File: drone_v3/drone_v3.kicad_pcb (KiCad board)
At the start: 2 copper layers, 47.5 x 47.5 mm, 85 parts, among them J1 USB_B_Micro, J10 Conn_01x08_Male, J12 Conn_01x08_Male, J13 Conn_01x08_Male, J14 Conn_01x02_Male, J15 UART4_con, J16 Conn_01x03_Male, J17 Conn_01x02_Male, J18 Conn_01x03_Male, J19 Micro_SD_Card, J2 Conn_01x10_Female, J3 UART4_con, J4 Conn_01x04_Male, J5 Conn_01x02_Female, J6 Conn_01x04_Male, J7 Conn_01x04_Male, J8 UART4_con, J9 Conn_01x06_Male, Q1 2N3904, Q2 2N3904, SW1 SW_Push, U1 STM32F405RGTx, U2 USBLC6-2SC6, U3 MPU-9250, U4 MCP1700-3302E_SOT23, U5 24LC512, U6 NRF24L01_Breakout, U7 MS5611-01BA, U8 ICM-20602, U9 MCP1700-3302E_SOT23, Y1 Crystal_GND24

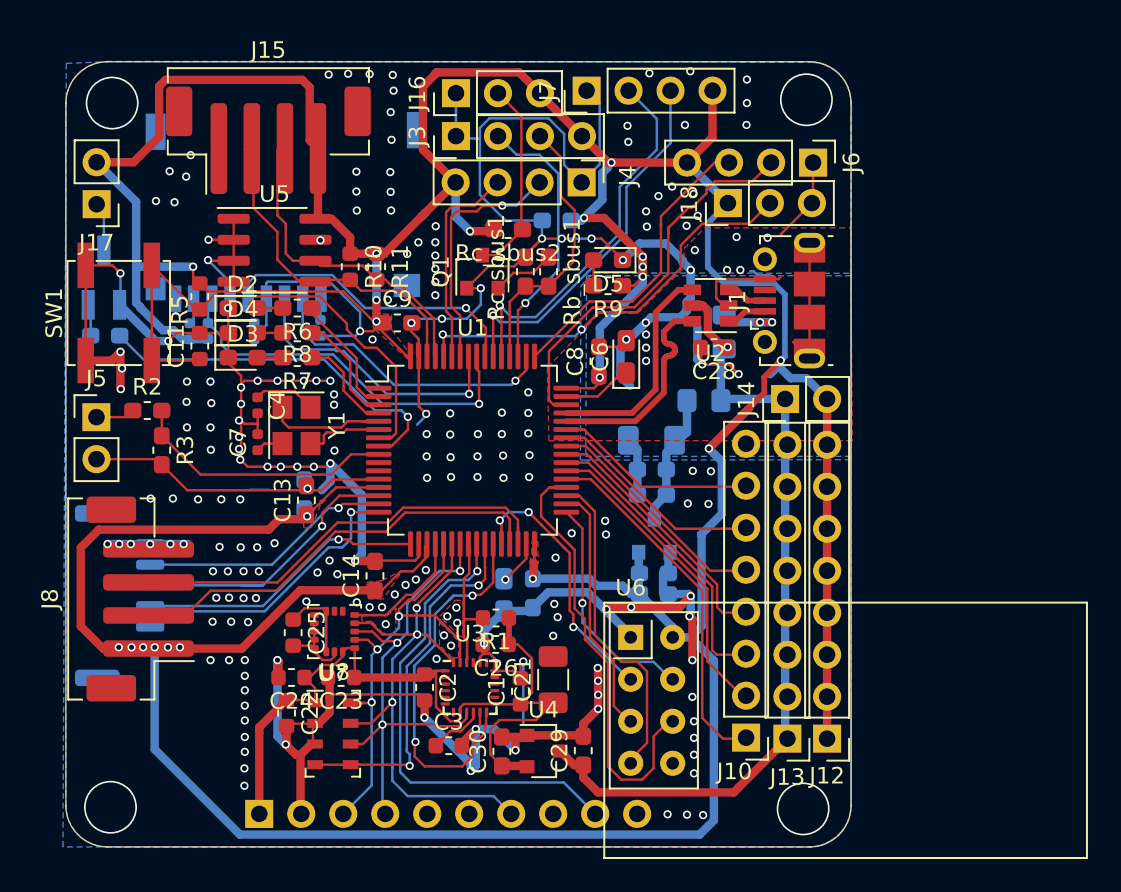
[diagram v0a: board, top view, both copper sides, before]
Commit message: cystal layout
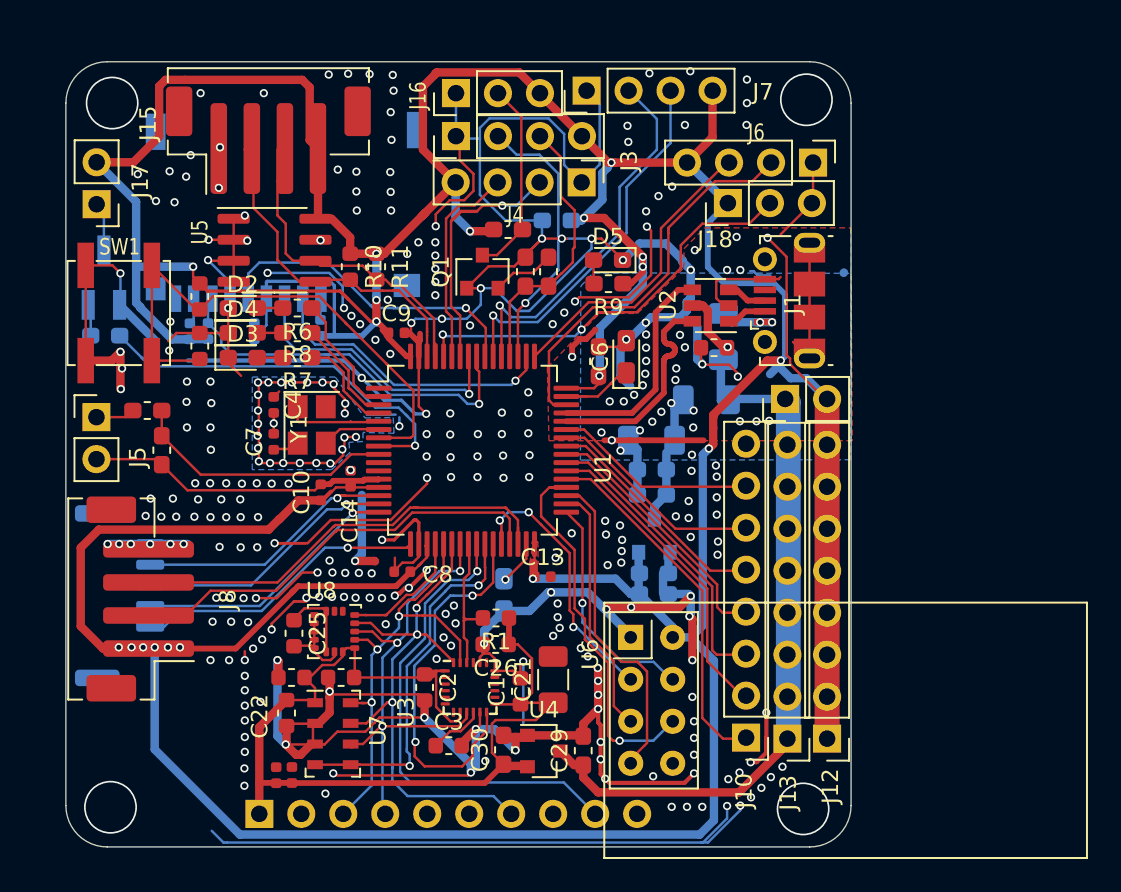
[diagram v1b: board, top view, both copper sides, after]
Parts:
- added C27: 1uF, Capacitor_SMD:C_0402_1005Metric, F.Cu at (118.7, 125.7)
- added C31: 100nF, Capacitor_SMD:C_0402_1005Metric, F.Cu at (117.7, 125.7)
- C10: footprint Capacitor_SMD:C_0603_1608Metric_Pad1.05x0.95mm_HandSolder -> Capacitor_SMD:C_0402_1005Metric; moved to F.Cu
- C13, C14, C8, C9: footprint Capacitor_SMD:C_0603_1608Metric_Pad1.05x0.95mm_HandSolder -> Capacitor_SMD:C_0402_1005Metric
- C20: moved to F.Cu
- D1, D6: footprint Diode_SMD:D_0805_2012Metric_Pad1.15x1.40mm_HandSolder -> Diode_SMD:D_1206_3216Metric
- moved C8 17.4 mm to (125.3, 113.3), turned to 180 degrees
- moved C13 15.0 mm to (133.8, 113.7), turned to 0 degrees
- moved C20 14.6 mm to (137.2, 100.6), turned to 90 degrees
- moved G*** 8.81 mm to (136.8, 104.0)
- moved C14 6.06 mm to (122.2, 107.7)
- moved C10 1.01 mm to (120.4, 108.5)
- moved C7 0.98 mm to (117.6, 105.5)
- moved C4 0.98 mm to (117.6, 103.3)
- moved Y1 0.93 mm to (119.9, 104.5)
- moved C9 0.60 mm to (125.0, 98.9)
- moved D6 0.28 mm to (144.8, 99.1)
- moved D1 0.16 mm to (143.8, 103.0)
- moved C30 0.14 mm to (131.5, 124.1)
- moved R9 0.13 mm to (137.8, 95.9)
- moved C25 0.06 mm to (118.8, 117.1)
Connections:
- J1 pad 6: Net-(J1-Pad6) -> GND
- J9 pad 2: UART2_TX -> UART2_RX
- J9 pad 3: UART2_RX -> UART2_TX
- J9 pad 4: UART2_CTS -> UART2_RTS
- J9 pad 5: UART2_RTS -> UART2_CTS
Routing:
- net GND: track 297.3 -> 479.4 mm, vias 211 -> 311
- net +3.3VA: track 49.3 -> 62.1 mm
- net Net-(J1-Pad6): track 7.21 -> 0.00 mm
- net VCC: track 315.4 -> 320.4 mm, vias 22 -> 19
- net SPI2_MOSI: track 27.4 -> 23.4 mm, vias 0 -> 1
- net Net-(C4-Pad1): track 3.94 -> 0.64 mm
- net OSC1+: track 7.96 -> 5.01 mm
- net Buzzer: track 22.4 -> 24.8 mm
- net NRST: track 32.0 -> 34.2 mm
- net SD_CLK: track 18.9 -> 20.9 mm
- net UART2_CTS: track 17.7 -> 15.7 mm
- net UART2_TX: track 17.6 -> 16.3 mm
- net (no net): track 1.33 -> 0.03 mm
- net OSC1-: track 4.81 -> 3.58 mm
- net Net-(C15-Pad1): track 7.99 -> 6.97 mm
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
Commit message: crystal layout
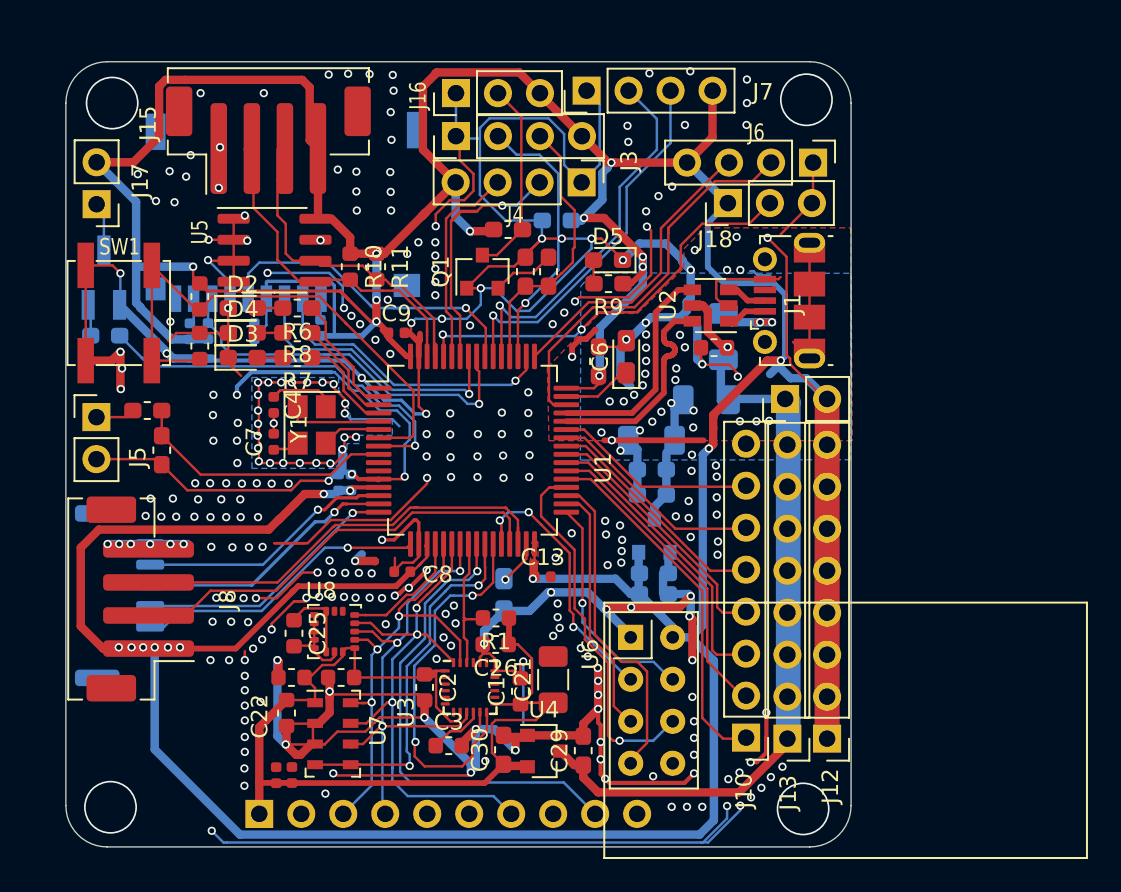
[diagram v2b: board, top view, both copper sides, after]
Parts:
- C10, C14: moved to B.Cu
- moved C10 1.23 mm to (121.5, 108.0)
- moved C14 0.23 mm to (122.2, 108.0)
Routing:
- net GND: track 479.4 -> 501.8 mm, vias 311 -> 313
- net Net-(C4-Pad1): track 0.64 -> 4.69 mm
- net VCC: track 320.4 -> 320.7 mm, vias 19 -> 21

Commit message: change 20602 to 20948, ms5611 to bmp180
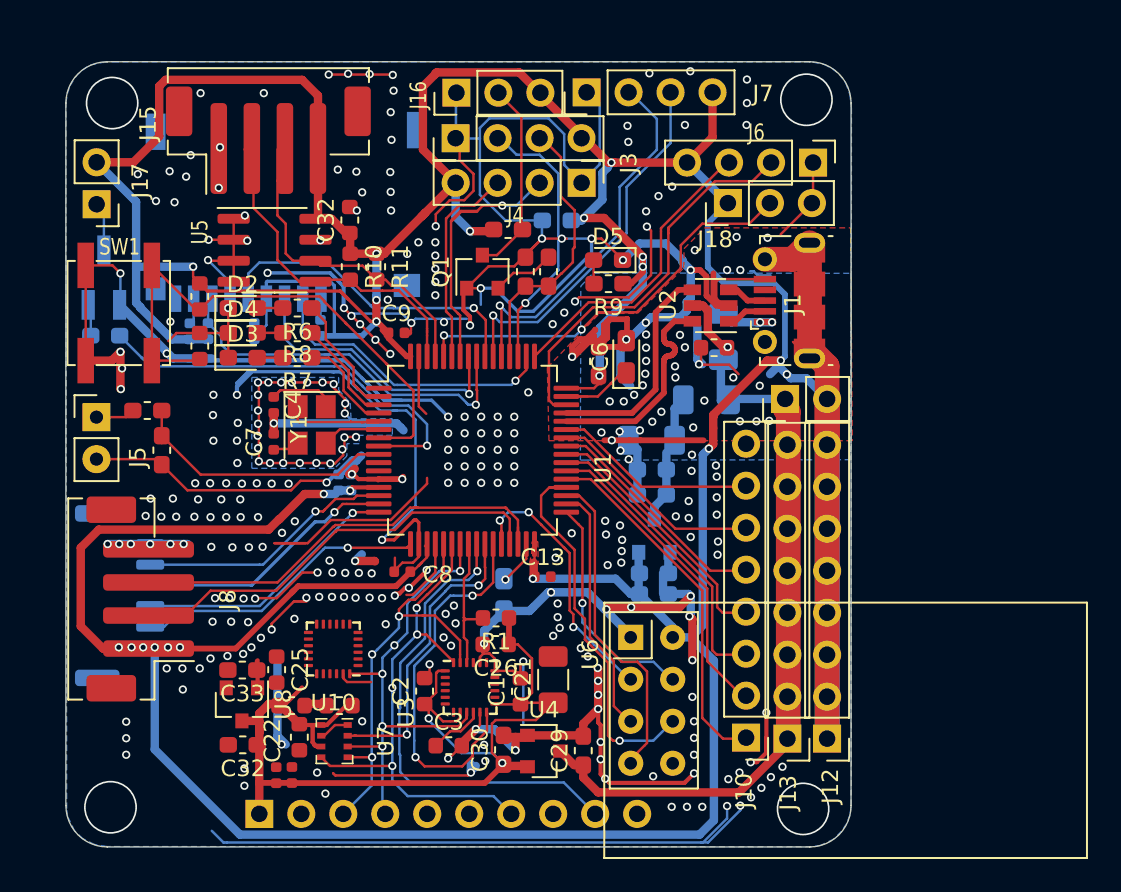
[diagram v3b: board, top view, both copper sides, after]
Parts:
- added C32: 1uF, Capacitor_SMD:C_0603_1608Metric_Pad1.05x0.95mm_HandSolder, F.Cu at (115.7, 123.8)
- added C32: C, Capacitor_SMD:C_0603_1608Metric, F.Cu at (122.2, 92.1)
- added C33: 1uF, Capacitor_SMD:C_0603_1608Metric_Pad1.05x0.95mm_HandSolder, F.Cu at (115.7, 119.3)
- added U10: ICM-20948, Sensor_Motion:InvenSense_QFN-24_3x3mm_P0.4mm, F.Cu at (121.2, 118.0)
- U7: value MS5611-01BA -> BMP280; footprint Package_LGA:LGA-8_3x5mm_P1.25mm -> Package_LGA:Bosch_LGA-8_2x2.5mm_P0.65mm_ClockwisePinNumbering
- U8: value ICM-20602 -> MCP1804x-1802xDB; footprint Package_LGA:LGA-16_3x3mm_P0.5mm_LayoutBorder3x5y -> Package_TO_SOT_SMD:SOT-23
- moved G*** 11.2 mm to (125.6, 103.7)
- moved U8 7.12 mm to (115.7, 121.4), turned to 270 degrees
- moved C25 2.44 mm to (117.8, 119.3)
- moved C23 1.70 mm to (121.5, 121.5)
- moved C24 1.70 mm to (118.7, 121.5), turned to 0 degrees
- moved C22 1.66 mm to (119.1, 123.4)
- moved U7 0.46 mm to (121.2, 123.6), turned to 270 degrees
- moved C2 0.23 mm to (126.7, 120.6), turned to 90 degrees
- moved J3 0.13 mm to (128.6, 87.1)
- moved J7 0.10 mm to (136.5, 84.3)
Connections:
- C25 pad 2: Net-(C25-Pad2) -> GND
- U1 pad 10: Net-(U1-Pad10) -> ADC1
- U1 pad 44: USB_D+ -> USB_D-
- U1 pad 45: USB_D- -> USB_D+
- U1 pad 9: ADC1 -> Net-(U1-Pad9)
- U2 pad 4: USB_D- -> USB_D+
- U2 pad 6: USB_D+ -> USB_D-
- U7 pad 1: +3.3VA -> GND
- U7 pad 2: GND -> IMU_CS3
- U7 pad 3: GND -> IMU_MOSI
- U7 pad 4: IMU_CS3 -> IMU_CLK
- U7 pad 5: IMU_CS3 -> IMU_MISO
- U7 pad 6: IMU_MOSI -> +3.3VA
- U7 pad 7: IMU_MISO -> GND
- U7 pad 8: IMU_CLK -> +3.3VA
- U8 pad 1: +3.3VA -> +1V8
- U8 pad 2: IMU_CLK -> GND
- U8 pad 3: IMU_MOSI -> +3.3VA
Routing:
- net GND: track 501.8 -> 537.3 mm, vias 313 -> 323
- net Net-(C25-Pad2): track 5.36 -> 0.00 mm
- net +3.3VA: track 62.1 -> 67.3 mm, vias 0 -> 2
- net Net-(C25-Pad1): track 4.80 -> 0.00 mm
- net IMU_CS3: track 23.6 -> 19.0 mm
- net IMU_CS2: track 8.53 -> 4.80 mm
- net IMU_MISO: track 34.0 -> 31.4 mm, vias 3 -> 4
- net +1V8: track 0.00 -> 2.20 mm
- net IMU_MOSI: track 32.7 -> 31.1 mm, vias 3 -> 5
- net Buzzer: track 24.7 -> 26.2 mm
- net OSC1+: track 5.01 -> 5.93 mm
- net SD_MISO: track 23.8 -> 24.5 mm
- net I2C_SCl: track 20.2 -> 19.5 mm
- net SD_CS: track 19.0 -> 18.4 mm

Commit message: add icm20948
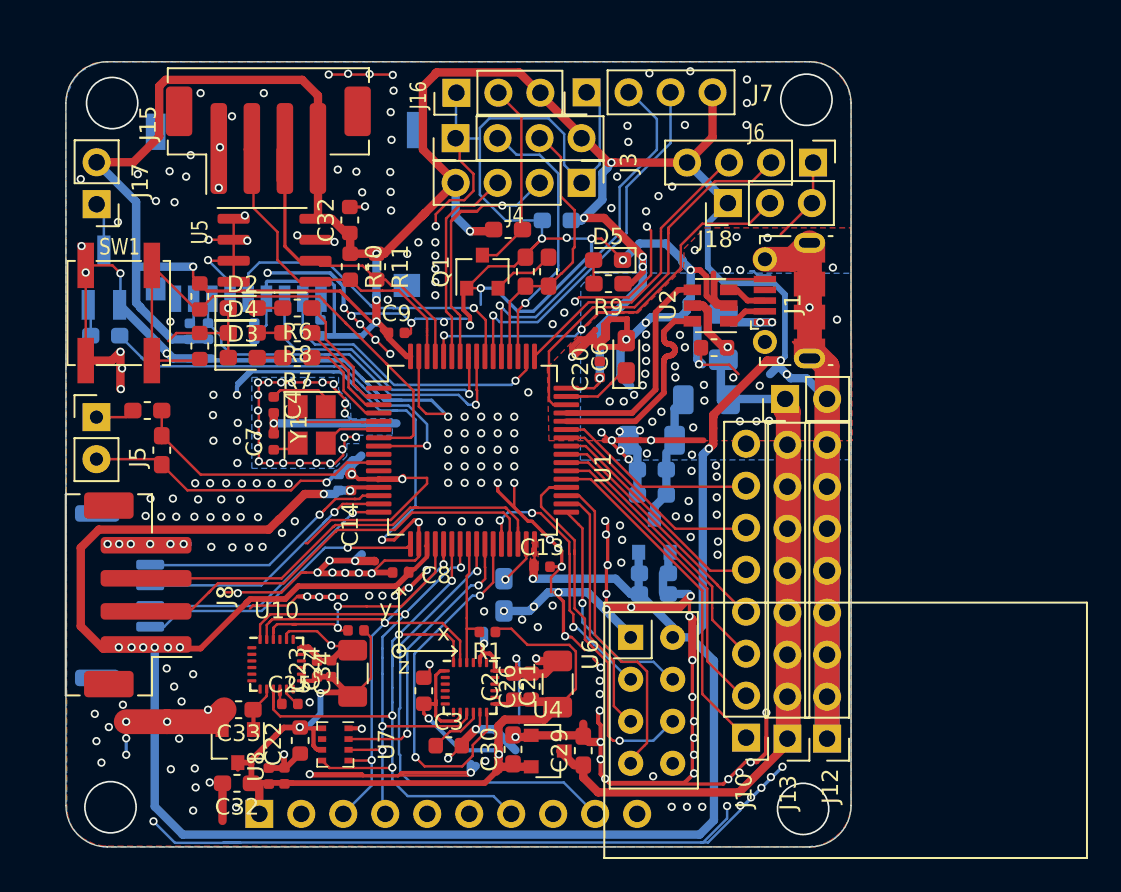
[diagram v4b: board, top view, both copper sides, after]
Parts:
- added C34: CP, Capacitor_SMD:C_1206_3216Metric, F.Cu at (122.3, 119.5)
- added R16: R, Resistor_SMD:R_0402_1005Metric, F.Cu at (122.5, 116.9)
- added x: indicator, drone_v3:indicator, F.Cu at (125.2, 118.2)
- C14: moved to F.Cu
- C20: footprint Capacitor_SMD:C_0603_1608Metric_Pad1.05x0.95mm_HandSolder -> Capacitor_SMD:C_0402_1005Metric
- C23, C24, C25: footprint Capacitor_SMD:C_0603_1608Metric -> Capacitor_SMD:C_0402_1005Metric
- R1: footprint Resistor_SMD:R_0603_1608Metric -> Resistor_SMD:R_0402_1005Metric
- moved C1 5.85 mm to (126.7, 120.5)
- moved C2 5.41 mm to (132.1, 120.3)
- moved U10 3.55 mm to (117.8, 119.0), turned to 0 degrees
- moved C26 3.34 mm to (133.2, 120.3), turned to 90 degrees
- moved C24 3.28 mm to (121.0, 119.2), turned to 90 degrees
- moved C23 2.59 mm to (120.2, 119.2), turned to 90 degrees
- moved U8 2.54 mm to (115.4, 123.9)
- moved C33 2.41 mm to (115.5, 121.7)
- moved C32 2.35 mm to (115.3, 126.2)
- moved C25 2.22 mm to (118.5, 121.3), turned to 0 degrees
- moved R1 1.00 mm to (130.5, 117.0)
- moved C13 0.60 mm to (133.8, 113.0)
- moved C30 0.58 mm to (132.1, 124.1)
- moved C20 0.50 mm to (137.3, 101.1)
- moved C27 0.45 mm to (118.2, 125.7)
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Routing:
- net GND: track 537.3 -> 637.0 mm, vias 323 -> 338
- net +3.3VA: track 67.3 -> 85.8 mm, vias 2 -> 4
- net IMU_MISO: track 31.4 -> 44.4 mm
- net IMU_CS2: track 4.80 -> 16.6 mm, vias 0 -> 2
- net IMU_CLK: track 29.3 -> 37.3 mm
- net IMU_MOSI: track 31.1 -> 38.8 mm, vias 5 -> 4
- net VCC: track 320.7 -> 325.4 mm
- net I2C_SCl: track 19.5 -> 21.1 mm
- net Net-(C25-Pad1): track 0.00 -> 1.19 mm
- net TIM3_CH3: track 17.7 -> 16.8 mm
- net IMU_INT: track 23.0 -> 22.2 mm
- net TIM3_CH1: track 21.7 -> 21.0 mm
- net TIM3_CH4: track 15.4 -> 14.8 mm
- net +1V8: track 2.20 -> 2.80 mm
- net IMU1_CS: track 29.2 -> 28.7 mm

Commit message: repair drc
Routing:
- net GND: track 637.0 -> 635.6 mm
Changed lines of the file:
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@@
     (thickness 1.6)
     (drawings 10)
-    (tracks 1942)
+    (tracks 1940)
     (zones 0)
     (modules 94)
@@
   (segment (start 139.575 105.95) (end 139.025 105.4) (width 0.508) (layer B.Cu) (net 1))
   (segment (start 139.575 108.7) (end 139.575 105.95) (width 0.508) (layer B.Cu) (net 1))
-  (segment (start 147.6 101.4) (end 148.1 100.9) (width 0.508) (layer B.Cu) (net 1))
   (segment (start 149.795999 101.645999) (end 151.05 102.9) (width 0.508) (layer B.Cu) (net 1))
   (segment (start 148.845999 101.645999) (end 149.795999 101.645999) (width 0.508) (layer B.Cu) (net 1))
-  (segment (start 148.1 100.9) (end 148.6125 101.4125) (width 0.508) (layer B.Cu) (net 1))
   (segment (start 140.404491 97.958009) (end 142.172557 97.958009) (width 0.508) (layer B.Cu) (net 1))
   (via (at 121.9 103.175) (size 0.5) (drill 0.3) (layers F.Cu B.Cu) (net 1))

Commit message: add alot
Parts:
- 3.3 CLK DIO GND: renamed from J6
- 3.3 RX1 TX1 GND: renamed from J4
- C5: moved to F.Cu
- C6: value CP -> VCAP
- U7: value BMP280 -> BMP388; footprint Package_LGA:Bosch_LGA-8_2x2.5mm_P0.65mm_ClockwisePinNumbering -> drone_v3:PQFN50P200X200X80-10N
- moved x 0.56 mm to (124.7, 117.9)
- moved PWM 0.45 mm to (145.7, 123.4)
- moved D6 0.38 mm to (144.8, 98.8)
- moved D1 0.25 mm to (143.5, 103.0)
- moved 5v 0.25 mm to (148.4, 123.5)
- moved C18 0.24 mm to (140.4, 114.9)
- moved C5 0.21 mm to (131.7, 114.7)
- moved U7 0.15 mm to (121.4, 123.9), turned to 90 degrees
- moved C13 0.10 mm to (133.8, 113.2)
- moved C14 0.10 mm to (122.2, 107.8)
- moved C27 0.08 mm to (118.3, 125.7)
- moved C32 0.07 mm to (115.3, 126.2)
- turned C22 to 90 degrees
- renumbered R10 to 1k, U5 to 24LC512, J13 to 5v, J5 to BAT, J18 to BOOT, J17 to Buzzer, U2 to ESD, J12 to GND, J15 to I2C, U10 to ICM-20948, U4 to MCP1700, U8 to MCP1804, SW1 to NRST, J10 to PWM, D5 to PWR, J16 to SBUS, U1 to STM32F405, J8 to UART3, J3 to UART4, U6 to nRF24
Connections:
- C15 pad 1: Net-(C15-Pad1) -> PWR_IN
- C16 pad 1: Net-(C15-Pad1) -> PWR_IN
- C17 pad 1: Net-(C15-Pad1) -> PWR_IN
- D1 pad 2: Net-(C15-Pad1) -> PWR_IN
- D6 pad 2: +5V -> PWR_IN
- U7 pad 1: GND -> +3.3VA
- U7 pad 2: IMU_CS3 -> IMU_CLK
- U7 pad 3: IMU_MOSI -> GND
- U7 pad 4: IMU_CLK -> IMU_MOSI
- U7 pad 6: +3.3VA -> IMU_CS3
- U7 pad 7: GND -> Net-(U7-Pad7)
- U7 pad 8: +3.3VA -> GND
- U9 pad 3: Net-(C15-Pad1) -> PWR_IN
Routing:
- net +5V: track 48.8 -> 24.9 mm, vias 1 -> 0
- net GND: track 635.6 -> 657.6 mm, vias 338 -> 342
- net PWR_IN: track 0.00 -> 11.0 mm
- net Net-(C15-Pad1): track 6.97 -> 0.00 mm
- net +3.3VA: track 85.8 -> 91.2 mm
- net VCAP_1: track 2.68 -> 5.18 mm, vias 1 -> 0
- net IMU_MISO: track 44.4 -> 43.7 mm
- net IMU_CLK: track 37.3 -> 37.9 mm
- net UART1_TX: track 14.8 -> 14.3 mm
- net SWCLK: track 18.2 -> 18.8 mm

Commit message: fix via
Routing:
- net IMU_CS: track 8.31 -> 3.82 mm
- net IMU_INT: track 22.2 -> 18.7 mm
- net UART1_TX: track 14.3 -> 17.7 mm
- net IMU_CS3: track 18.9 -> 16.2 mm
- net VCC: vias 21 -> 20
- net GND: vias 342 -> 328
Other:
- net class Default: via_dia 0.5 -> 0.6
